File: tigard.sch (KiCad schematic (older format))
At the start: 69 parts, among them J1 USB_C_Receptacle_USB2.0, J2 JTAG, J3 UART, J4 SPI, J5 SWD, J6 I2C, Q1 BSH103, SW1 SW_SP3T, SW2 SW_DPDT, U1 AP7365-18, U2 AP7365-33, U3 FT2232HQ, U4 93LC56BT-I/OT, U5 SN74LVC8T245, U6 SN74LVC8T245, Y1 12MHz

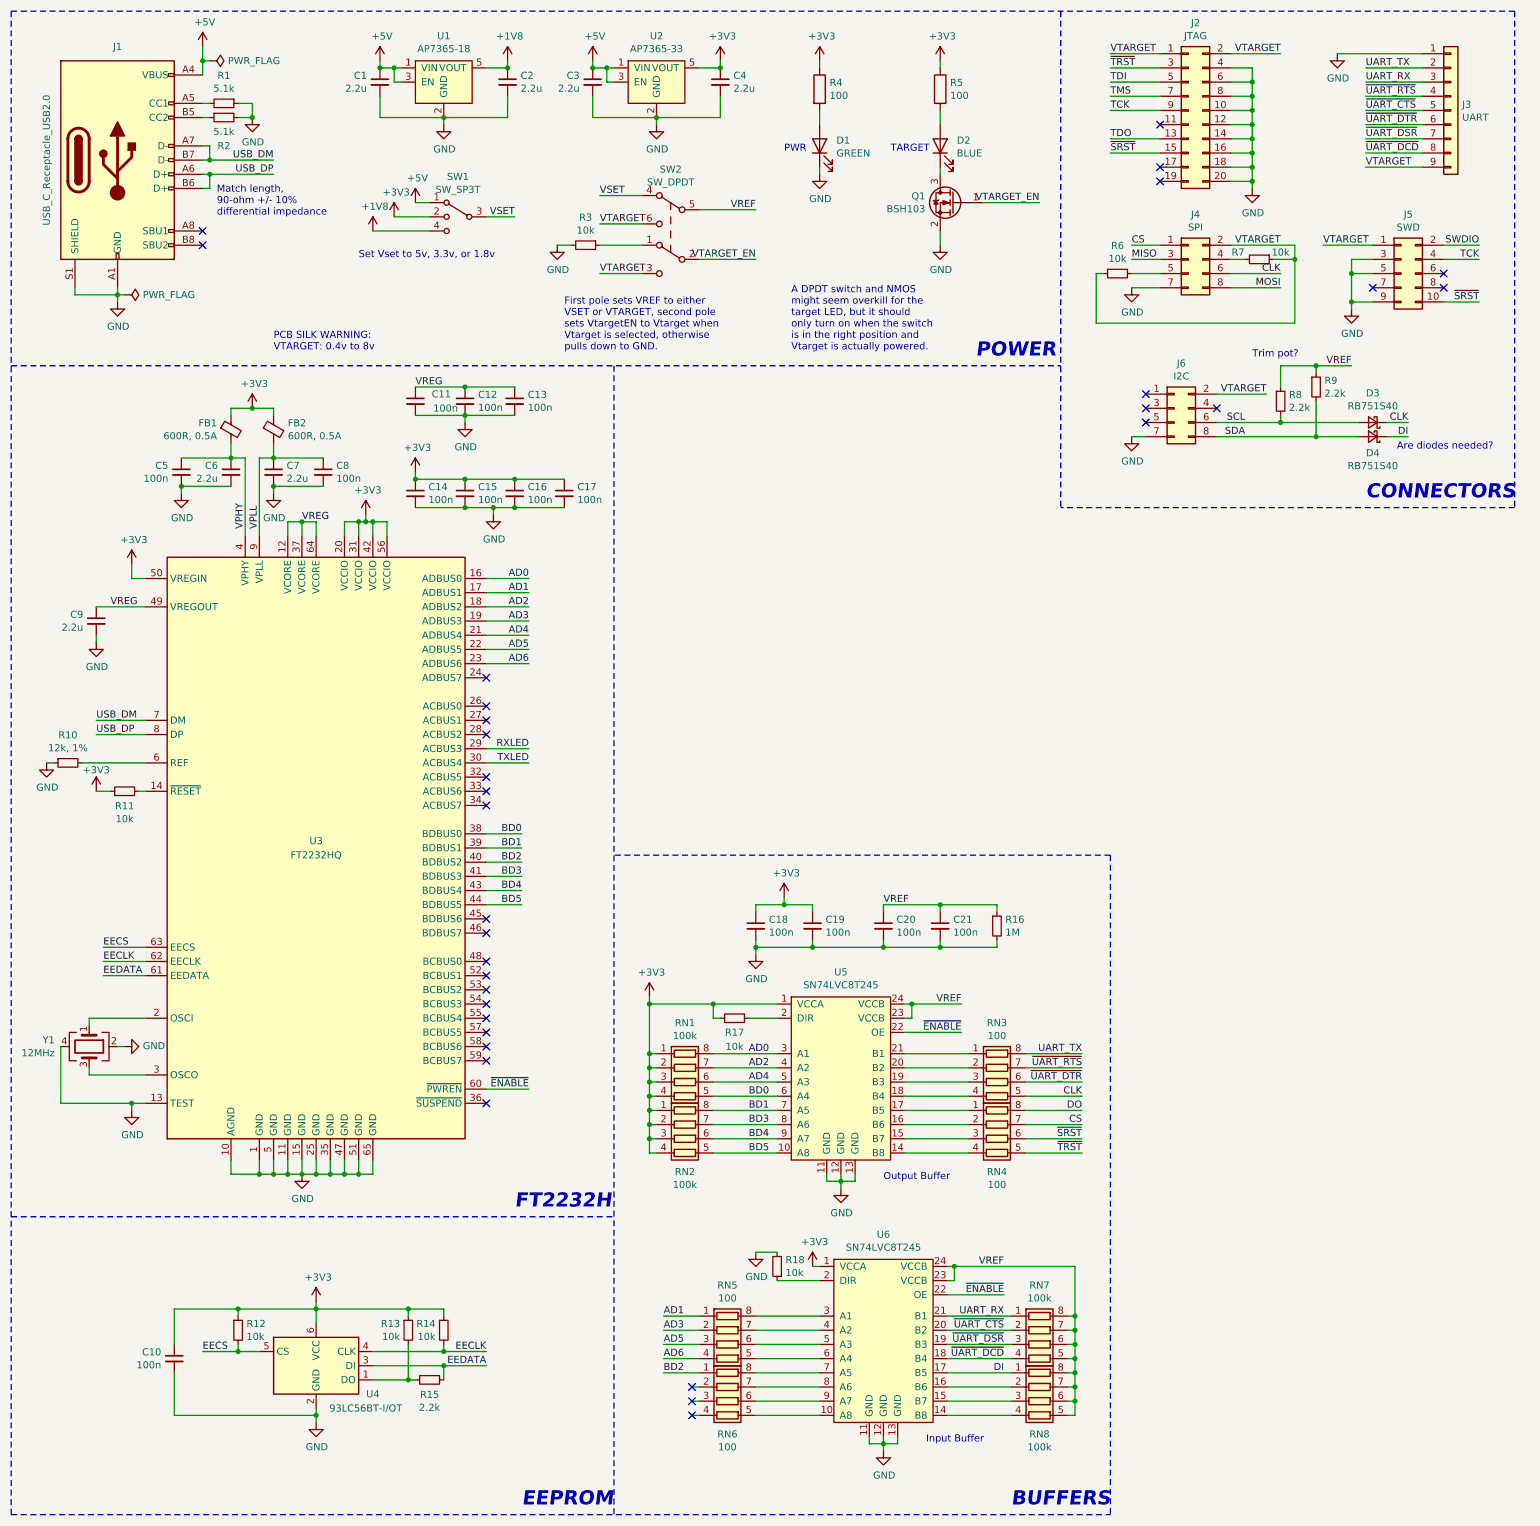
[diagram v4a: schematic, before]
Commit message: Add I2C/SWD switch, RX/TX and ENABLE LEDs
* Also adds another 2.2uF capacitor to VREGOUT
* Fixes some DRC complaints
* Adds aliases (wiring)
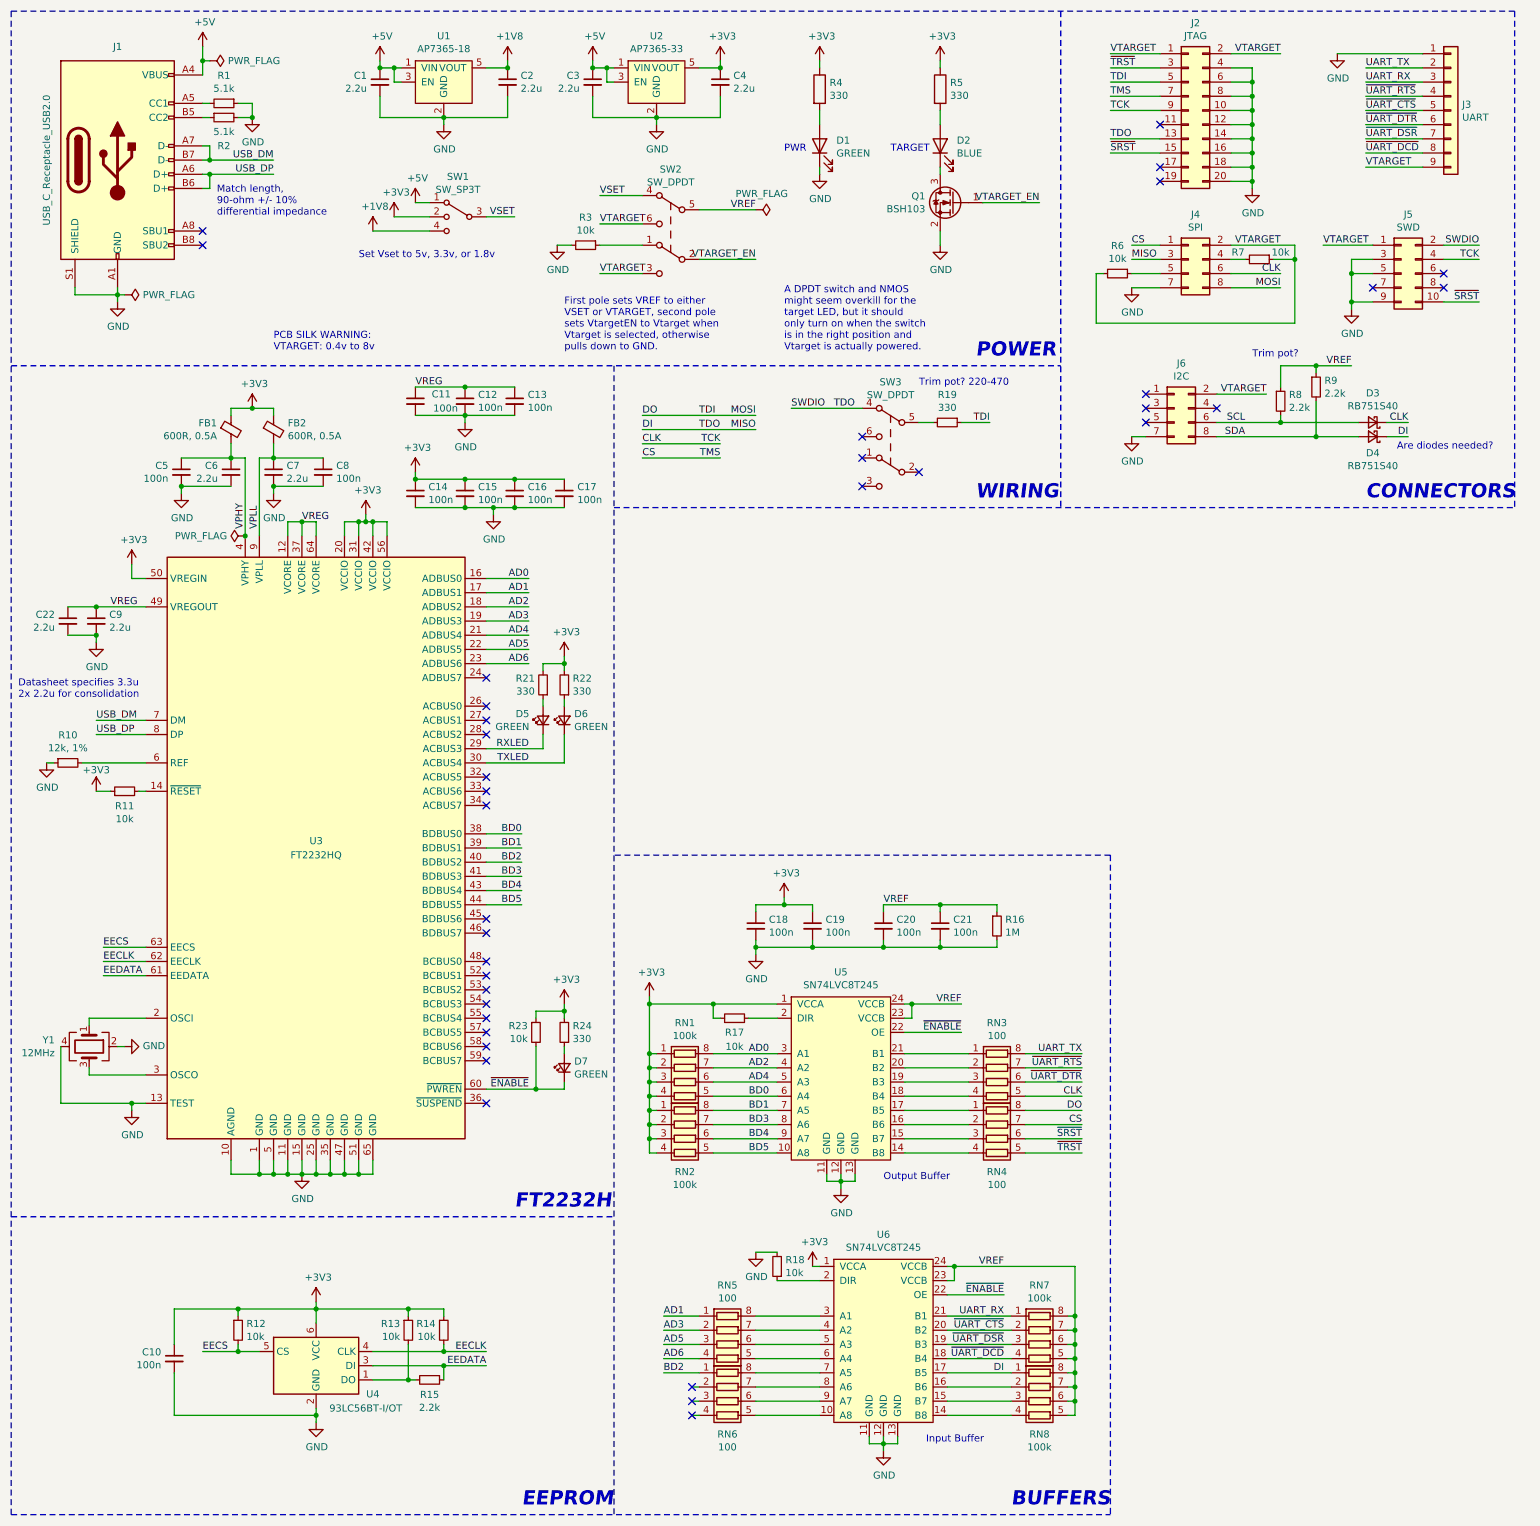
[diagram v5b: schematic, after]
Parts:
- added C22: 2.2u, Capacitor_SMD:C_0603_1608Metric, symbol Device:C_Small
- added D5, D6, D7: GREEN, LED_SMD:LED_0603_1608Metric, symbol Device:LED_Small
- added R19, R21, R22, R24: 330, Resistor_SMD:R_0402_1005Metric, symbol Device:R_Small
- added R23: 10k, Resistor_SMD:R_0402_1005Metric, symbol Device:R_Small
- added SW3: SW_DPDT, Button_Switch_THT:SW_CuK_JS202011CQN_DPDT_Straight, symbol tigard:SW_DPDT
- R4, R5: value 100 -> 330; LCSC C25138 -> C25104; P/N 0402WGJ0101TCE -> 0402WGF3300TCE
- U3: footprint Package_DFN_QFN:QFN-64-1EP_9x9mm_P0.5mm_EP4.35x4.35mm -> Package_DFN_QFN:QFN-64-1EP_9x9mm_P0.5mm_EP4.35x4.35mm_ThermalVias
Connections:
- net MISO is gone; now on net DI: J4.3 (Pin_3)
- net MOSI is gone; now on net DO: J4.8 (Pin_8)
- net SWDIO is gone; now on net DI: J5.2 (Pin_2)
- net TCK is gone; now on net CLK: J2.9 (Pin_9), J5.4 (Pin_4)
- net TDI is gone; now on net DO: J2.5 (Pin_5)
- net TDO is gone; now on net DI: J2.13 (Pin_13)
- net TMS is gone; now on net CS: J2.7 (Pin_7)
- net +3V3: now also R21.2, R22.2, R23.1, R24.2
- net DI: now also SW3.4
- net DO: now also R19.1
- net GND: now also C22.2
- net RXLED: now also D5.1 (K)
- net TXLED: now also D6.1 (K)
- net VREG: now also C22.1
- net ~ENABLE: now also D7.1 (K), R23.2
- new net: R19.2, SW3.5
- new net: D5.2 (A), R21.1
- new net: D6.2 (A), R22.1
- new net: D7.2 (A), R24.1
- no-connect marks 33 -> 37
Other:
- note added: "Datasheet specifies 3.3u\n2x 2.2u for consolidation"
- note added: "Trim pot? 220-470"
- note added: "WIRING"

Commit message: Add missing part numbers for FT2232HQ
* Also add csv# to .gitignore for libreoffice CSV temp files
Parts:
- U3: LCSC (none) -> C193662; P/N (none) -> FT2232HQ-REEL
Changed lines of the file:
@@
 F 2 "Package_DFN_QFN:QFN-64-1EP_9x9mm_P0.5mm_EP4.35x4.35mm_ThermalVias" H 2700 6450 50  0001 C CNN
 F 3 "https://www.ftdichip.com/Support/Documents/DataSheets/ICs/DS_FT2232H.pdf" H 2700 6450 50  0001 C CNN
+F 4 "FT2232HQ-REEL" H 2700 6450 50  0001 C CNN "P/N"
+F 5 "C193662" H 2700 6450 50  0001 C CNN "LCSC"
 	1    2700 6450
 	1    0    0    -1

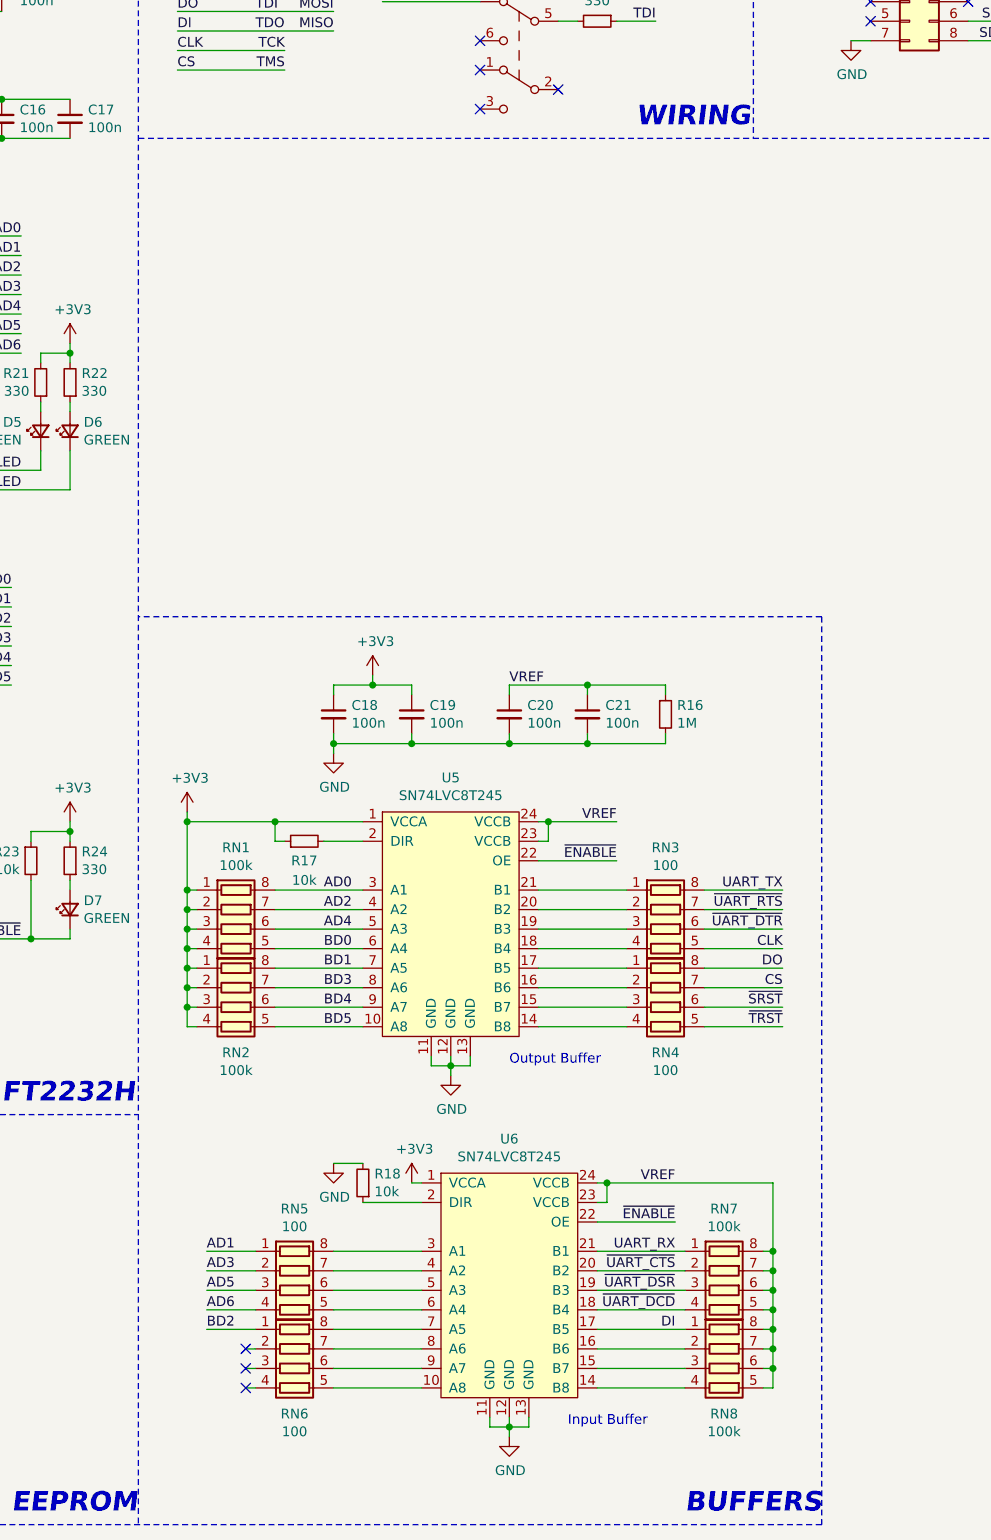
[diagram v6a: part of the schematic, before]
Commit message: Add mounting holes to schematic
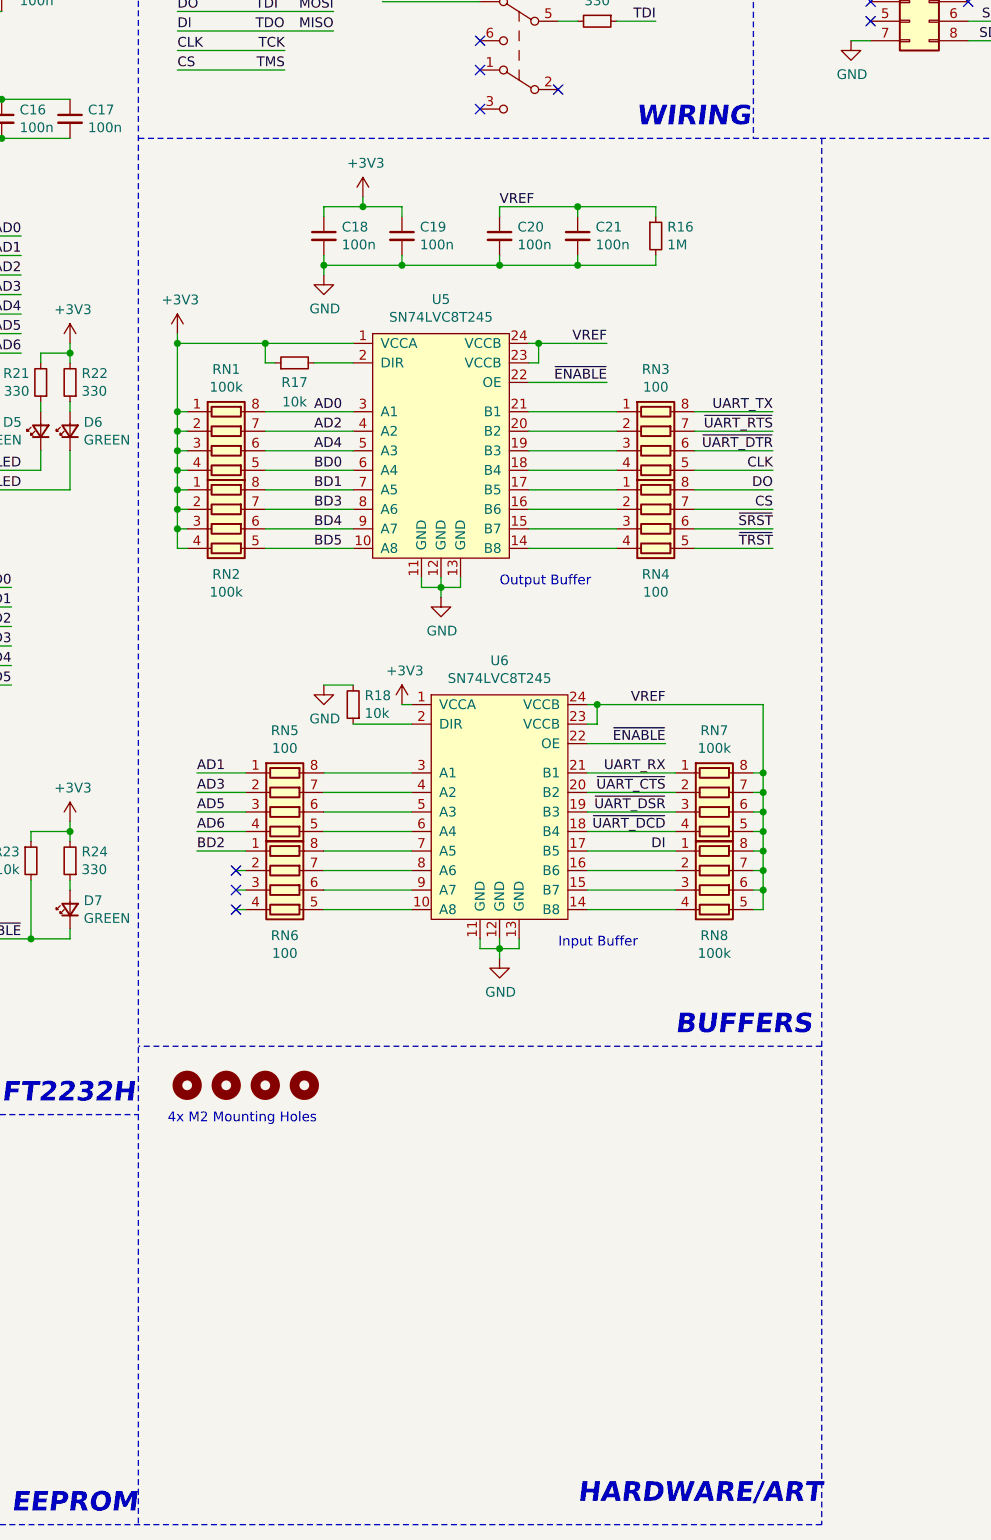
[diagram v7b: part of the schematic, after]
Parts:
- added H1, H2, H3, H4: MountingHole, MountingHole:MountingHole_2.2mm_M2, symbol Mechanical:MountingHole
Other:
- note added: "4x M2 Mounting Holes"
- note added: "HARDWARE/ART"
- moved on the sheet: C18, C19, C20, C21, R16, R17, R18, RN1, RN2, RN3, RN4, RN5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
